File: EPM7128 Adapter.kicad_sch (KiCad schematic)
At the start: 17 parts

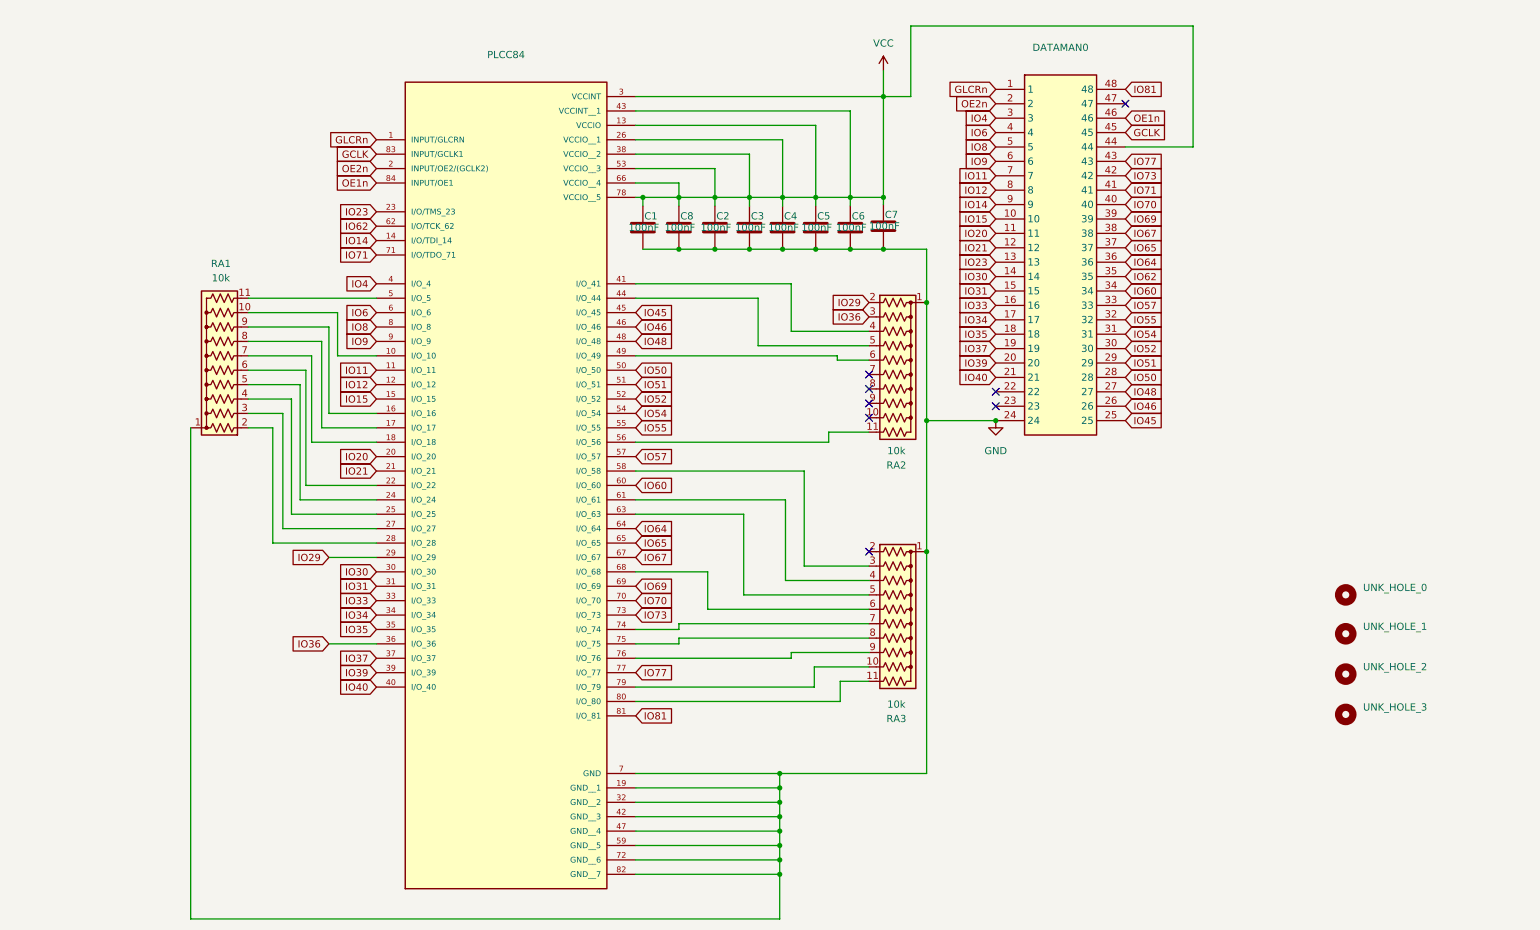
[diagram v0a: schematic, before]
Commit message: Add files via upload
Correct issue with lack of Gnd connection to JTAG, RNETs and PLCC Socket.
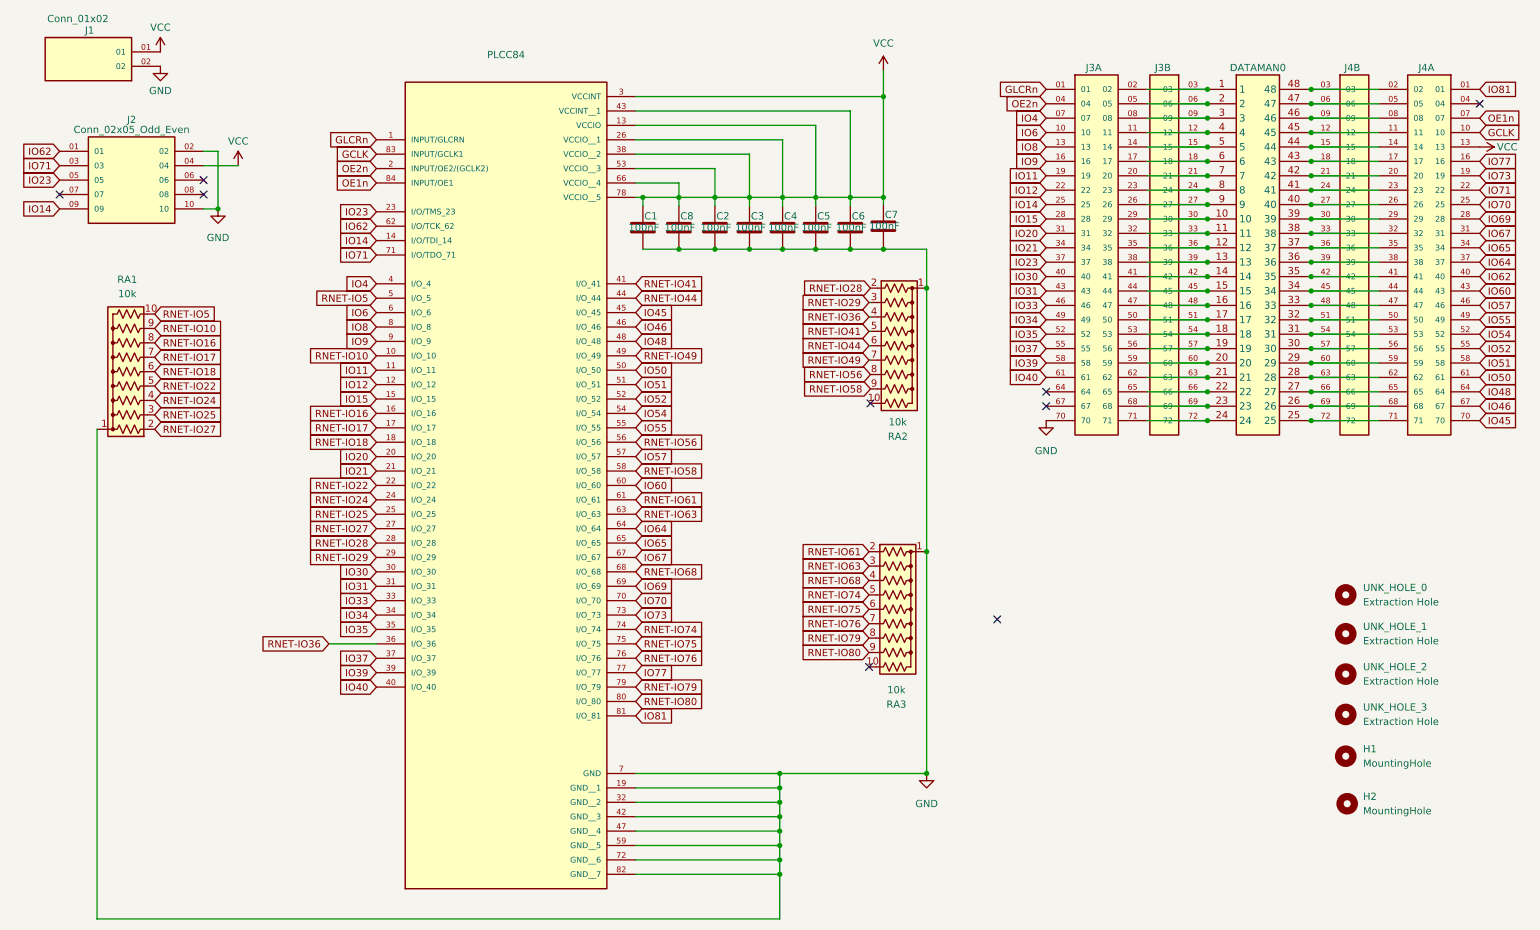
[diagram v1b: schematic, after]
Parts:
- added H1, H2: MountingHole, MountingHole:MountingHole_2.7mm_M2.5, symbol Mechanical:MountingHole
- added J1: Conn_01x02, Mod:SAMTEC_TSW-102-07-G-S, symbol EPM7128S_Adapter:TSW-102-07-G-S
- added J2: Conn_02x05_Odd_Even, Mod:SAMTEC_TSW-105-07-L-D, symbol EPM7128S_Adapter:TSW-105-07-L-D
- added J3, J4: TSW-124-08-T-T, Mod:SAMTEC_TSW-124-08-T-T, symbol EPM7128S_Adapter:TSW-124-08-T-T
- DATAMAN0: value ~ -> Pin-Pin Headers 1x24; Height (none) -> 4.2
- PLCC84: footprint S84 -> Mod:PLCC84AT
- RA1, RA2, RA3: footprint Resistor_THT:R_Array_SIP11 -> Mod:4610M101103LF; symbol EPM7128S_Adapter:R_Network10_US -> EPM7128S_Adapter:R_Network09_US
- UNK_HOLE_0: value ~ -> Extraction Hole; footprint dummyfp0 -> MountingHole:MountingHole_2.7mm_M2.5
- UNK_HOLE_1: value ~ -> Extraction Hole; footprint dummyfp1 -> MountingHole:MountingHole_2.7mm_M2.5
- UNK_HOLE_2: value ~ -> Extraction Hole; footprint dummyfp2 -> MountingHole:MountingHole_2.7mm_M2.5
- UNK_HOLE_3: value ~ -> Extraction Hole; footprint dummyfp3 -> MountingHole:MountingHole_2.7mm_M2.5
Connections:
- net GCLK: now also J4.10; no longer DATAMAN0.45
- net GLCRn: now also J3.01; no longer DATAMAN0.1
- net GND: now also J1.02, J2.02, J2.10, J3.70; no longer DATAMAN0.24
- net IO11: now also J3.19; no longer DATAMAN0.7
- net IO12: now also J3.22; no longer DATAMAN0.8
- net IO14: now also J2.09, J3.25; no longer DATAMAN0.9
- net IO15: now also J3.28; no longer DATAMAN0.10
- net IO20: now also J3.31; no longer DATAMAN0.11
- net IO21: now also J3.34; no longer DATAMAN0.12
- net IO23: now also J2.05, J3.37; no longer DATAMAN0.13
- net IO30: now also J3.40; no longer DATAMAN0.14
- net IO31: now also J3.43; no longer DATAMAN0.15
- net IO33: now also J3.46; no longer DATAMAN0.16
- net IO34: now also J3.49; no longer DATAMAN0.17
- net IO35: now also J3.52; no longer DATAMAN0.18
- net IO37: now also J3.55; no longer DATAMAN0.19
- net IO39: now also J3.58; no longer DATAMAN0.20
- net IO4: now also J3.07; no longer DATAMAN0.3
- net IO40: now also J3.61; no longer DATAMAN0.21
- net IO45: now also J4.70; no longer DATAMAN0.25
- net IO46: now also J4.67; no longer DATAMAN0.26
- net IO48: now also J4.64; no longer DATAMAN0.27
- net IO50: now also J4.61; no longer DATAMAN0.28
- net IO51: now also J4.58; no longer DATAMAN0.29
- net IO52: now also J4.55; no longer DATAMAN0.30
- net IO54: now also J4.52; no longer DATAMAN0.31
- net IO55: now also J4.49; no longer DATAMAN0.32
- net IO57: now also J4.46; no longer DATAMAN0.33
- net IO6: now also J3.10; no longer DATAMAN0.4
- net IO60: now also J4.43; no longer DATAMAN0.34
- net IO62: now also J2.01, J4.40; no longer DATAMAN0.35
- net IO64: now also J4.37; no longer DATAMAN0.36
- net IO65: now also J4.34; no longer DATAMAN0.37
- net IO67: now also J4.31; no longer DATAMAN0.38
- net IO69: now also J4.28; no longer DATAMAN0.39
- net IO70: now also J4.25; no longer DATAMAN0.40
- net IO71: now also J2.03, J4.22; no longer DATAMAN0.41
- net IO73: now also J4.19; no longer DATAMAN0.42
- net IO77: now also J4.16; no longer DATAMAN0.43
- net IO8: now also J3.13; no longer DATAMAN0.5
- net IO81: now also J4.01; no longer DATAMAN0.48
- net IO9: now also J3.16; no longer DATAMAN0.6
- net OE1n: now also J4.07; no longer DATAMAN0.46
- net OE2n: now also J3.04; no longer DATAMAN0.2
- net VCC: now also J1.01, J2.04, J4.13; no longer DATAMAN0.44
- net at RA3.10 (R9): no longer PLCC84.79 (I/O_79)
- net RNET-IO80: now reaches PLCC84.80 (I/O_80)
- net RNET-IO80: now also RA3.9 (R8); no longer RA3.11 (R10)
- net RNET-IO61: now reaches RA3.2 (R1)
- net RNET-IO61: now also PLCC84.61 (I/O_61)
- net RNET-IO58: now reaches PLCC84.58 (I/O_58)
- net RNET-IO58: now also RA2.9 (R8); no longer RA3.3 (R2)
- net RNET-IO68: now reaches RA3.4 (R3)
- net RNET-IO68: now also PLCC84.68 (I/O_68); no longer PLCC84.61 (I/O_61)
- net RNET-IO63: now reaches PLCC84.63 (I/O_63)
- net RNET-IO63: now also RA3.3 (R2); no longer RA3.5 (R4)
- net RNET-IO75: now reaches RA3.6 (R5)
- net RNET-IO75: now also PLCC84.75 (I/O_75); no longer PLCC84.68 (I/O_68)
- net RNET-IO74: now reaches PLCC84.74 (I/O_74)
- net RNET-IO74: now also RA3.5 (R4); no longer RA3.7 (R6)
- net RNET-IO79: now reaches RA3.8 (R7)
- net RNET-IO79: now also PLCC84.79 (I/O_79); no longer PLCC84.75 (I/O_75)
- net RNET-IO76: now reaches PLCC84.76 (I/O_76)
- net RNET-IO76: now also RA3.7 (R6); no longer RA3.9 (R8)
- net at DATAMAN0.22: now also J3.65, J3.66
- net at DATAMAN0.23: now also J3.68, J3.69
- net at DATAMAN0.47: now also J4.05, J4.06
- net RNET-IO56: now reaches PLCC84.56 (I/O_56)
- net RNET-IO56: now also RA2.8 (R7); no longer RA2.11 (R10)
- net RNET-IO36: now reaches RA2.4 (R3)
- net RNET-IO36: now also PLCC84.36 (I/O_36); no longer PLCC84.41 (I/O_41)
- net RNET-IO41: now reaches RA2.5 (R4)
- net RNET-IO41: now also PLCC84.41 (I/O_41); no longer PLCC84.44 (I/O_44)
- net RNET-IO44: now reaches RA2.6 (R5)
- net RNET-IO44: now also PLCC84.44 (I/O_44); no longer PLCC84.49 (I/O_49)
- net RNET-IO49: now reaches RA2.7 (R6)
- net RNET-IO49: now also PLCC84.49 (I/O_49)
- net RNET-IO10: now reaches PLCC84.10 (I/O_10)
- net RNET-IO10: now also RA1.9 (R8); no longer RA1.10 (R9)
- net RNET-IO16: now reaches PLCC84.16 (I/O_16)
- net RNET-IO16: now also RA1.8 (R7); no longer RA1.9 (R8)
- net RNET-IO17: now reaches PLCC84.17 (I/O_17)
- net RNET-IO17: now also RA1.7 (R6); no longer RA1.8 (R7)
- net RNET-IO18: now reaches PLCC84.18 (I/O_18)
- net RNET-IO18: now also RA1.6 (R5); no longer RA1.7 (R6)
- net RNET-IO22: now reaches PLCC84.22 (I/O_22)
- net RNET-IO22: now also RA1.5 (R4); no longer RA1.6 (R5)
- net RNET-IO24: now reaches PLCC84.24 (I/O_24)
- net RNET-IO24: now also RA1.4 (R3); no longer RA1.5 (R4)
- net RNET-IO25: now reaches PLCC84.25 (I/O_25)
- net RNET-IO25: now also RA1.3 (R2); no longer RA1.4 (R3)
- net RNET-IO27: now reaches PLCC84.27 (I/O_27)
- net RNET-IO27: now also RA1.2 (R1); no longer RA1.3 (R2)
- net RNET-IO28: now reaches PLCC84.28 (I/O_28)
- net RNET-IO28: now also RA2.2 (R1); no longer RA1.2 (R1)
- net RNET-IO5: now reaches PLCC84.5 (I/O_5)
- net RNET-IO5: now also RA1.10 (R9); no longer RA1.11 (R10)
- net IO29 renamed RNET-IO29
- net RNET-IO29: now also RA2.3 (R2); no longer RA2.2 (R1)
- removed net IO36: PLCC84.36 (I/O_36), RA2.3 (R2)
- new net: DATAMAN0.1, J3.02, J3.03
- new net: DATAMAN0.10, J3.29, J3.30
- new net: DATAMAN0.11, J3.32, J3.33
- new net: DATAMAN0.12, J3.35, J3.36
- new net: DATAMAN0.13, J3.38, J3.39
- new net: DATAMAN0.14, J3.41, J3.42
- new net: DATAMAN0.15, J3.44, J3.45
- new net: DATAMAN0.16, J3.47, J3.48
- new net: DATAMAN0.17, J3.50, J3.51
- new net: DATAMAN0.18, J3.53, J3.54
- new net: DATAMAN0.19, J3.56, J3.57
- new net: DATAMAN0.2, J3.05, J3.06
- new net: DATAMAN0.20, J3.59, J3.60
- new net: DATAMAN0.21, J3.62, J3.63
- new net: DATAMAN0.24, J3.71, J3.72
- new net: DATAMAN0.25, J4.71, J4.72
- new net: DATAMAN0.26, J4.68, J4.69
- new net: DATAMAN0.27, J4.65, J4.66
- new net: DATAMAN0.28, J4.62, J4.63
- new net: DATAMAN0.29, J4.59, J4.60
- new net: DATAMAN0.3, J3.08, J3.09
- new net: DATAMAN0.30, J4.56, J4.57
- new net: DATAMAN0.31, J4.53, J4.54
- new net: DATAMAN0.32, J4.50, J4.51
- new net: DATAMAN0.33, J4.47, J4.48
- new net: DATAMAN0.34, J4.44, J4.45
- new net: DATAMAN0.35, J4.41, J4.42
- new net: DATAMAN0.36, J4.38, J4.39
- new net: DATAMAN0.37, J4.35, J4.36
- new net: DATAMAN0.38, J4.32, J4.33
- new net: DATAMAN0.39, J4.29, J4.30
- new net: DATAMAN0.4, J3.11, J3.12
- new net: DATAMAN0.40, J4.26, J4.27
- new net: DATAMAN0.41, J4.23, J4.24
- new net: DATAMAN0.42, J4.20, J4.21
- new net: DATAMAN0.43, J4.17, J4.18
- new net: DATAMAN0.44, J4.14, J4.15
- new net: DATAMAN0.45, J4.11, J4.12
- new net: DATAMAN0.46, J4.08, J4.09
- new net: DATAMAN0.48, J4.02, J4.03
- new net: DATAMAN0.5, J3.14, J3.15
- new net: DATAMAN0.6, J3.17, J3.18
- new net: DATAMAN0.7, J3.20, J3.21
- new net: DATAMAN0.8, J3.23, J3.24
- new net: DATAMAN0.9, J3.26, J3.27
- no-connect marks 8 -> 9
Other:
- moved on the sheet: DATAMAN0
